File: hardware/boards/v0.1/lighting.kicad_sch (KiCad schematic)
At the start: 18 parts, among them U10 TRIG9, U11 TRIG13, U12 TRIG10, U13 TRIG14, U14 TRIG11, U15 TRIG15, U16 TRIG12, U17 TRIG16, U2 TRIG1, U3 TRIG2, U33 SN74AHCT1G125DBVR, U4 TRIG3, U5 TRIG4, U6 TRIG8, U7 TRIG7, U8 TRIG6, U9 TRIG5

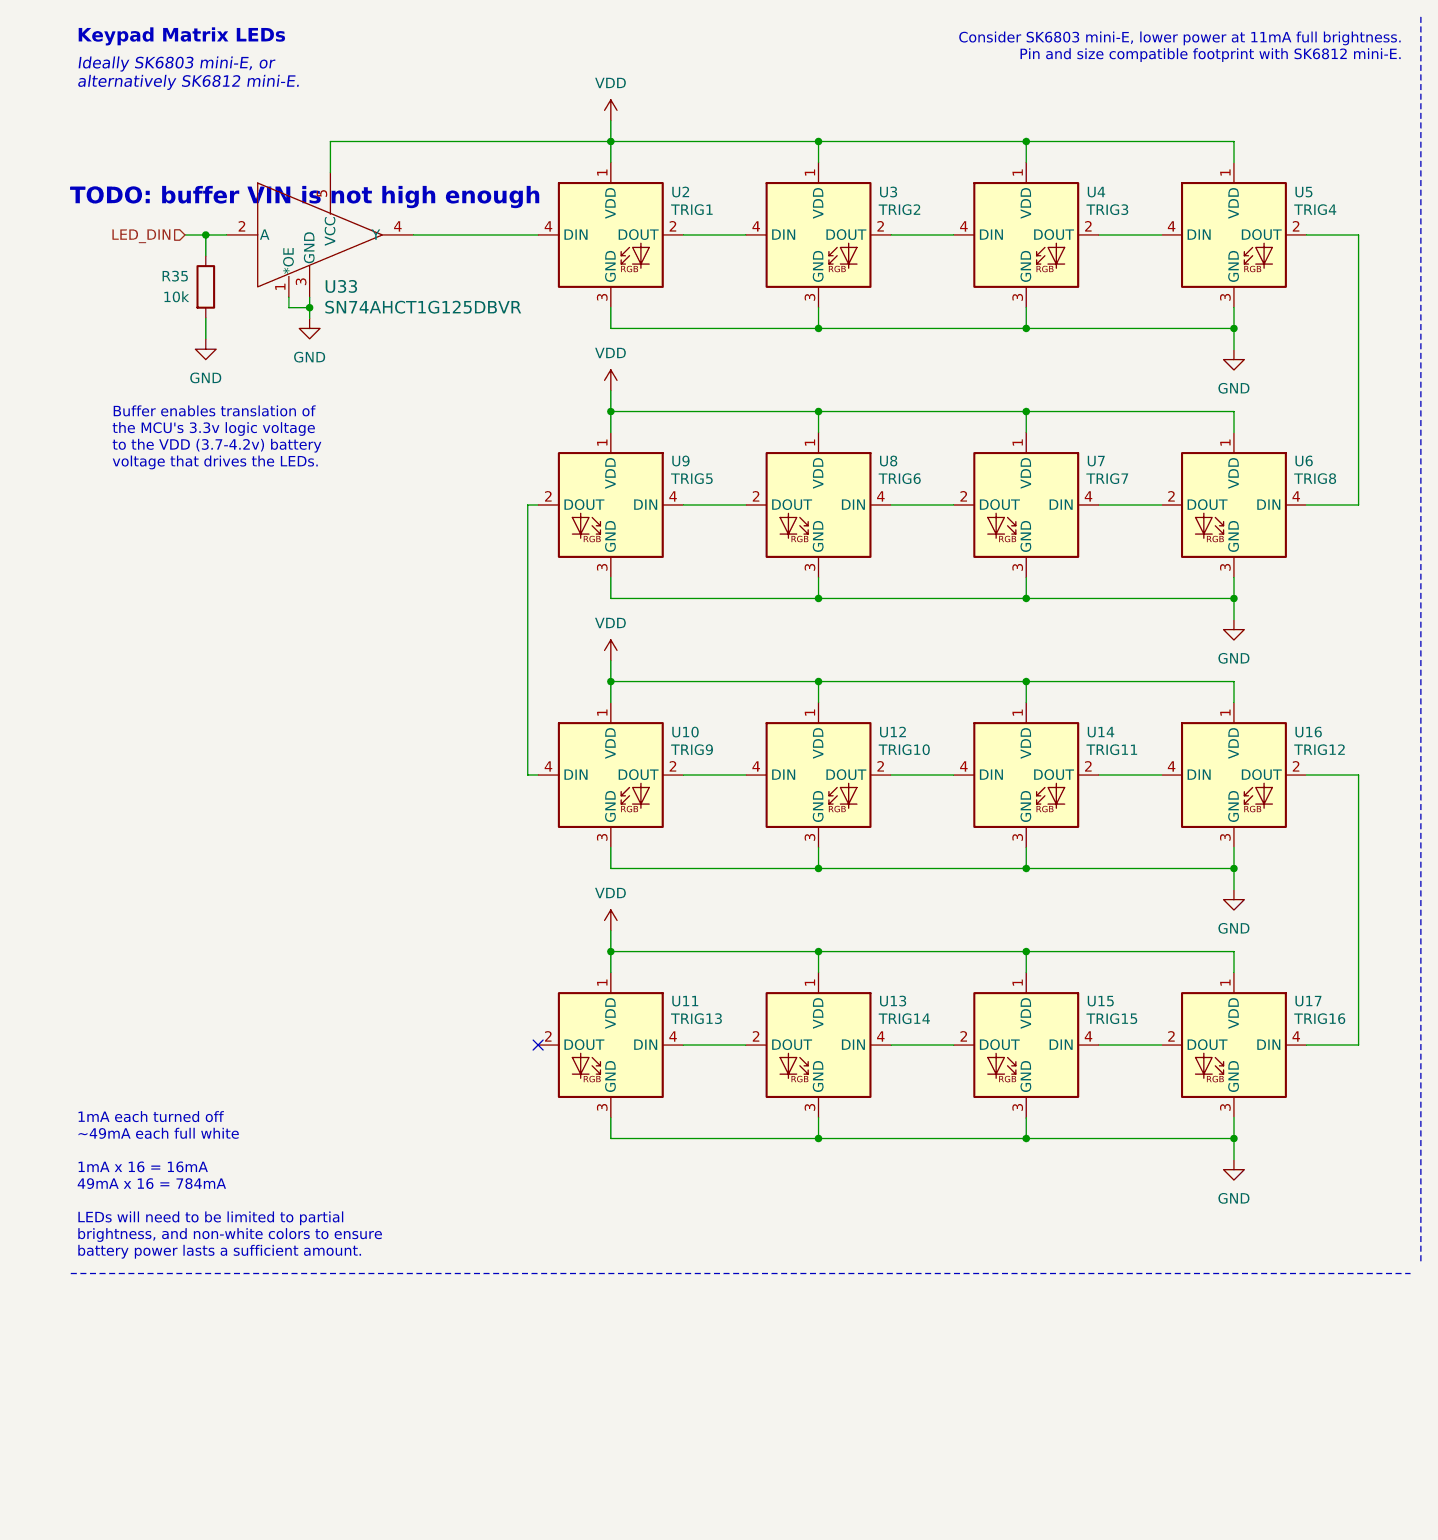
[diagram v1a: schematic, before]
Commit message: feat: fix RGB LED circuit
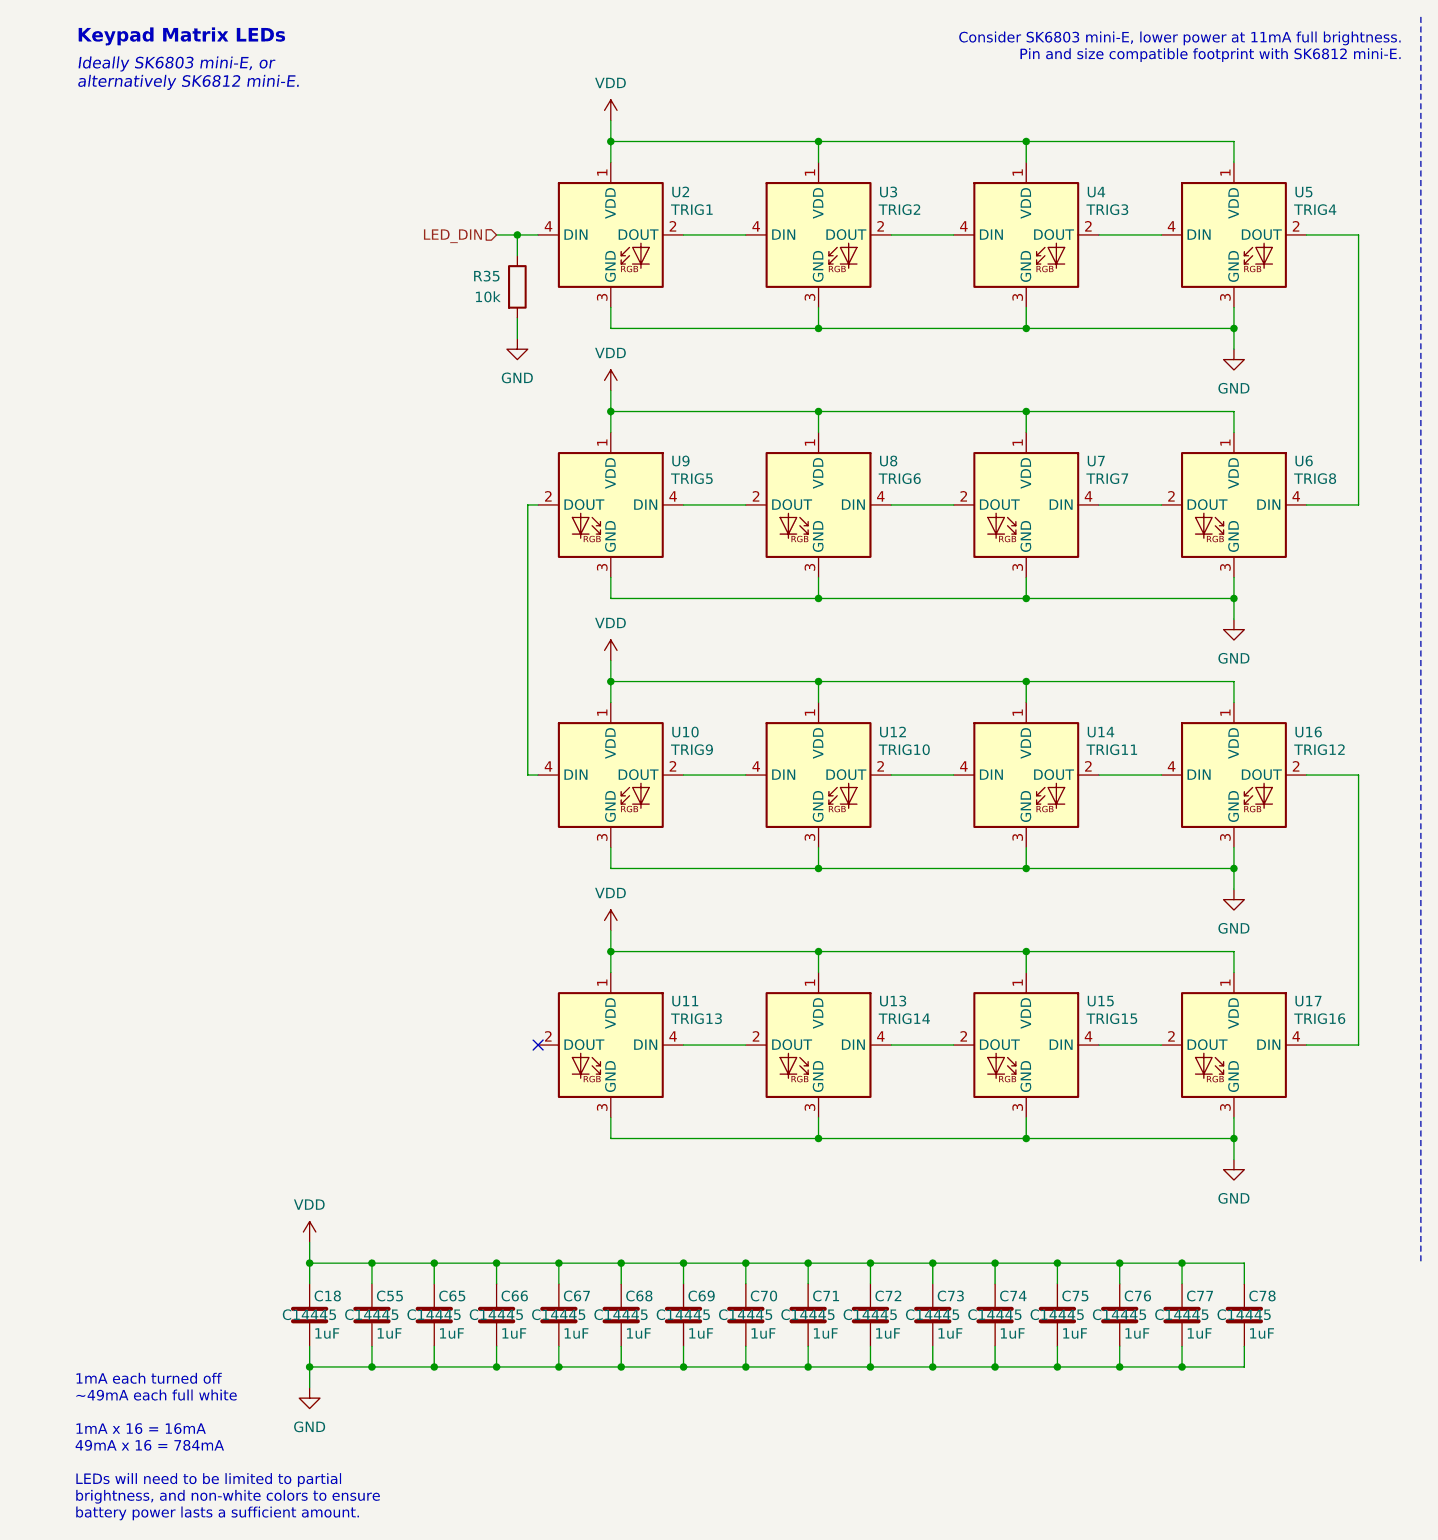
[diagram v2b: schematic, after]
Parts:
- removed U33: SN74AHCT1G125DBVR, pocket_synth:SN74AHCT1G125DBVR, symbol pocket_synth:SN74AHCT1G125DBVR
- added C18, C55, C65, C66, C67, C68, C69, C70, C71, C72, C73, C74, C75, C76, C77, C78: 1uF, Capacitor_SMD:C_0402_1005Metric, symbol Device:C
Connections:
- net GND: now also C18.2, C55.2, C65.2, C66.2, C67.2, C68.2, C69.2, C70.2, C71.2, C72.2, C73.2, C74.2, C75.2, C76.2, C77.2, C78.2
- net LED_DIN: now also U2.4 (DIN)
- net VDD: now also C18.1, C55.1, C65.1, C66.1, C67.1, C68.1, C69.1, C70.1, C71.1, C72.1, C73.1, C74.1, C75.1, C76.1, C77.1, C78.1
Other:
- note removed: "Buffer enables translation of the MCU's 3.3v logic voltage to the VDD (3.7-4.2v) battery voltage that drives the LEDs."
- note removed: "TODO: buffer VIN is not high enough"
- moved on the sheet: R35

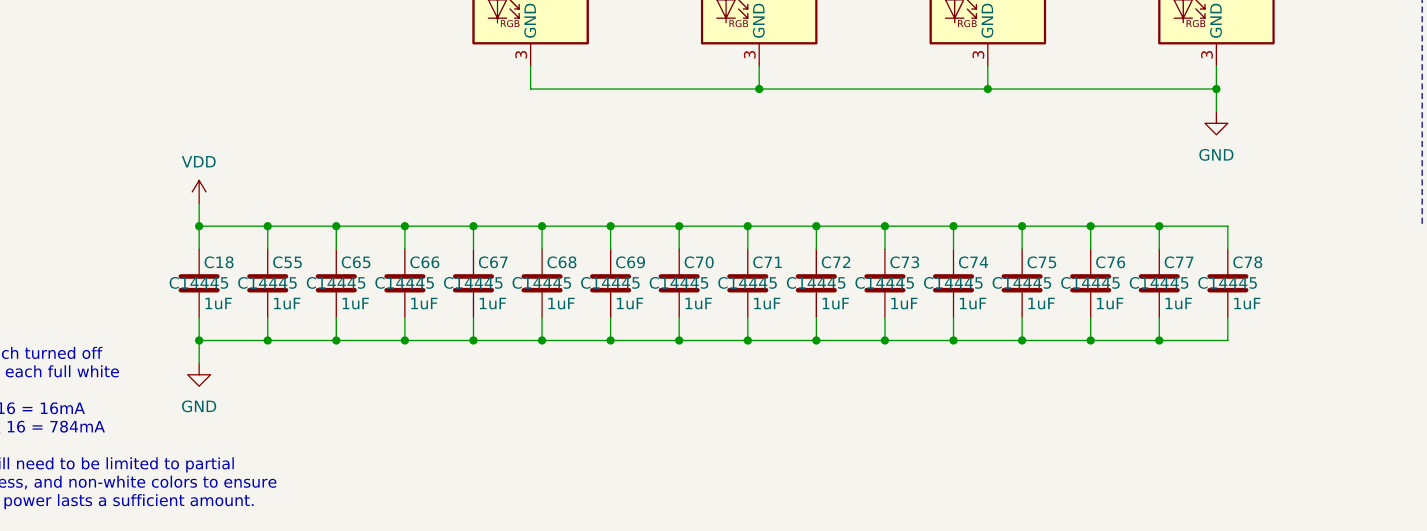
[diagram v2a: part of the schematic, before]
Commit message: feat: change charger, fuel gauge, and battery connector, re-route power system
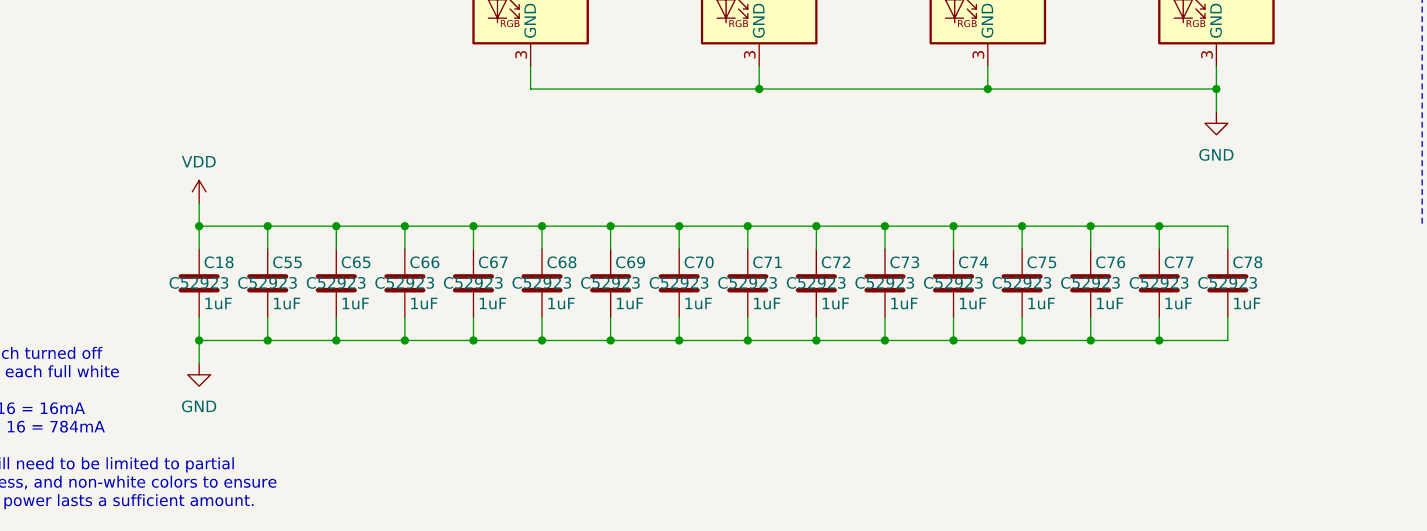
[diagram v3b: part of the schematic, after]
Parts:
- C18, C55, C65, C66, C67, C68, C69, C70, C71, C72, C73, C74, C75, C76, C77, C78: JLC C14445 -> C52923
- R35: JLC C25531 -> C25744
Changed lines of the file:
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@@
 			)
 		)
-		(property "JLC" "C14445"
+		(property "JLC" "C52923"
 			(at 125.73 171.45 0)
 			(effects
@@
 			)
 		)
-		(property "JLC" "C14445"
+		(property "JLC" "C52923"
 			(at 41.91 171.45 0)
 			(effects
@@
 			)
 		)
-		(property "JLC" "C14445"
+		(property "JLC" "C52923"
 			(at 140.97 171.45 0)
 			(effects
@@
 			)
 		)
-		(property "JLC" "C14445"
+		(property "JLC" "C52923"
 			(at 95.25 171.45 0)
 			(effects
@@
 			)
 		)
-		(property "JLC" "C14445"
+		(property "JLC" "C52923"
 			(at 80.01 171.45 0)
 			(effects
@@
 			)
 		)
-		(property "JLC" "C14445"
+		(property "JLC" "C52923"
 			(at 49.53 171.45 0)
 			(effects
@@
 			)
 		)
-		(property "JLC" "C14445"
+		(property "JLC" "C52923"
 			(at 118.11 171.45 0)
 			(effects
@@
 			)
 		)
-		(property "JLC" "C14445"
+		(property "JLC" "C52923"
 			(at 87.63 171.45 0)
 			(effects
@@
 			)
 		)
-		(property "JLC" "C14445"
+		(property "JLC" "C52923"
 			(at 110.49 171.45 0)
 			(effects
@@
 			)
 		)
-		(property "JLC" "C14445"
+		(property "JLC" "C52923"
 			(at 64.77 171.45 0)
 			(effects
@@
 			)
 		)
-		(property "JLC" "C14445"
+		(property "JLC" "C52923"
 			(at 57.15 171.45 0)
 			(effects
@@
 			)
 		)
-		(property "JLC" "C14445"
+		(property "JLC" "C52923"
 			(at 148.59 171.45 0)
 			(effects
@@
 			)
 		)
-		(property "JLC" "C14445"
+		(property "JLC" "C52923"
 			(at 156.21 171.45 0)
 			(effects
@@
 			)
 		)
-		(property "JLC" "C14445"
+		(property "JLC" "C52923"
 			(at 102.87 171.45 0)
 			(effects
@@
 			)
 		)
-		(property "JLC" "C14445"
+		(property "JLC" "C52923"
 			(at 133.35 171.45 0)
 			(effects
@@
 			)
 		)
-		(property "JLC" "C14445"
+		(property "JLC" "C52923"
 			(at 72.39 171.45 0)
 			(effects
@@
 			)
 		)
-		(property "JLC" "C25531"
+		(property "JLC" "C25744"
 			(at 67.31 45.72 0)
 			(effects

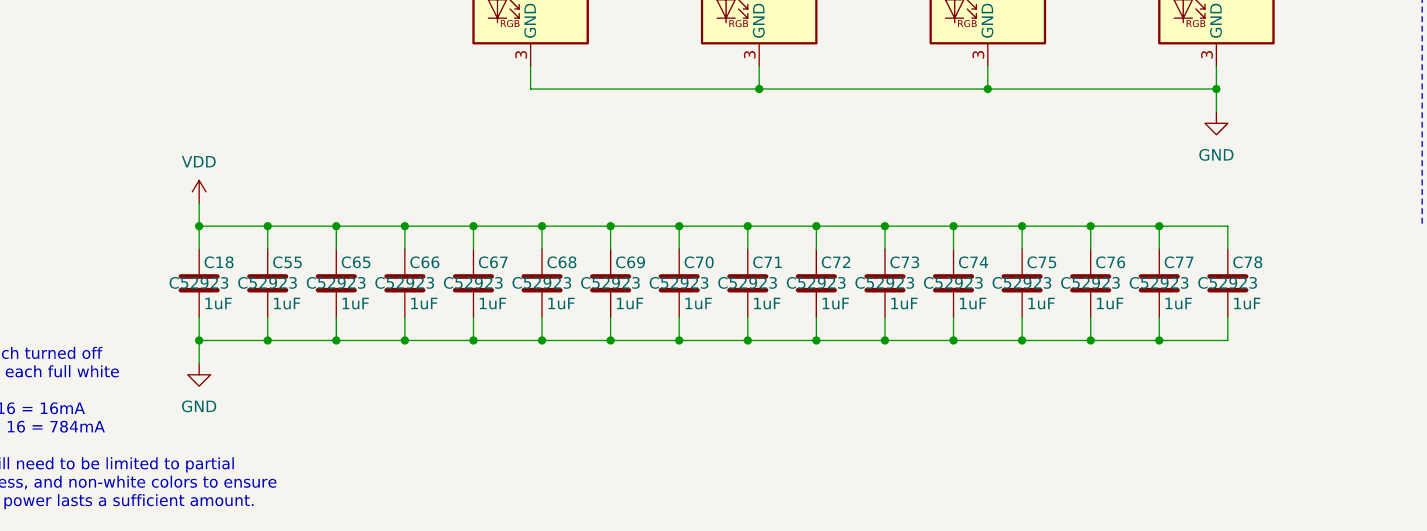
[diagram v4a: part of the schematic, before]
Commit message: feat: various layout and routing adjustments
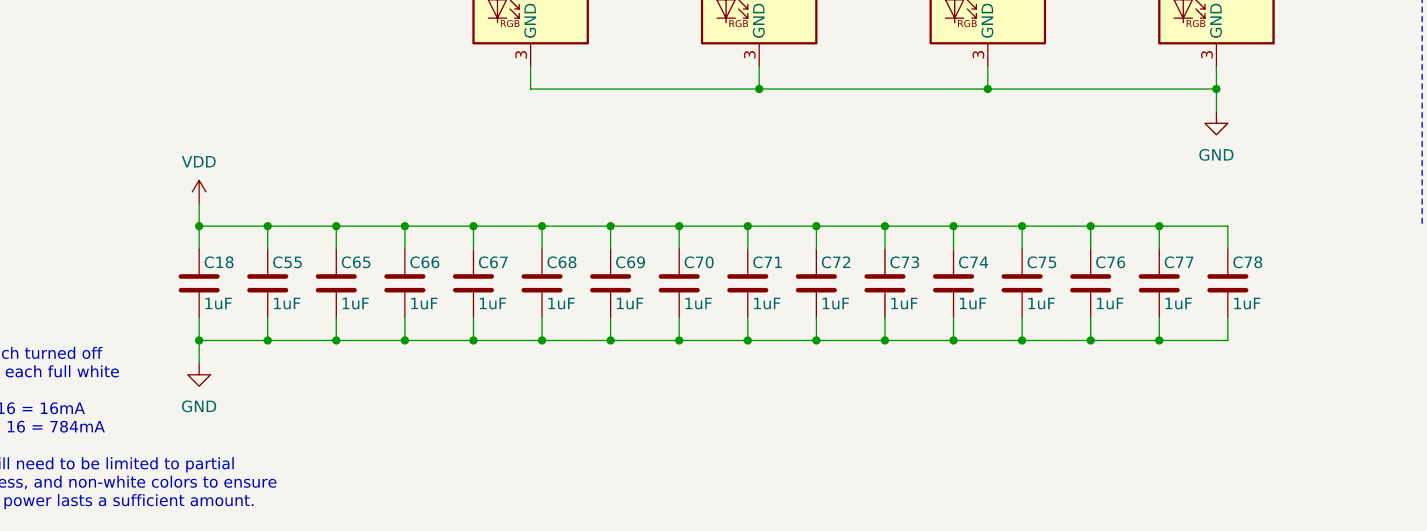
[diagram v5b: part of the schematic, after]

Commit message: fix: rotation offsets and LEDs on wrong side of board
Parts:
- U10, U11, U12, U13, U14, U15, U16, U17, U2, U3, U4, U5, U6, U7, U8, U9: FT Layer Override (none) -> bottom
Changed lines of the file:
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@@
 			)
 		)
+		(property "FT Layer Override" "bottom"
+			(at 104.14 72.39 0)
+			(effects
+				(font
+					(size 1.27 1.27)
+				)
+				(hide yes)
+			)
+		)
 		(pin "2"
 		)
@@
 			)
 		)
+		(property "FT Layer Override" "bottom"
+			(at 78.74 105.41 0)
+			(effects
+				(font
+					(size 1.27 1.27)
+				)
+				(hide yes)
+			)
+		)
 		(pin "2"
 		)
@@
 			)
 		)
+		(property "FT Layer Override" "bottom"
+			(at 154.94 39.37 0)
+			(effects
+				(font
+					(size 1.27 1.27)
+				)
+				(hide yes)
+			)
+		)
 		(pin "2"
 		)
@@
 			)
 		)
+		(property "FT Layer Override" "bottom"
+			(at 129.54 39.37 0)
+			(effects
+				(font
+					(size 1.27 1.27)
+				)
+				(hide yes)
+			)
+		)
 		(pin "2"
 		)
@@
 			)
 		)
+		(property "FT Layer Override" "bottom"
+			(at 129.54 138.43 0)
+			(effects
+				(font
+					(size 1.27 1.27)
+				)
+				(hide yes)
+			)
+		)
 		(pin "2"
 		)
@@
 			)
 		)
+		(property "FT Layer Override" "bottom"
+			(at 154.94 72.39 0)
+			(effects
+				(font
+					(size 1.27 1.27)
+				)
+				(hide yes)
+			)
+		)
 		(pin "2"
 		)
@@
 			)
 		)
+		(property "FT Layer Override" "bottom"
+			(at 78.74 138.43 0)
+			(effects
+				(font
+					(size 1.27 1.27)
+				)
+				(hide yes)
+			)
+		)
 		(pin "2"
 		)
@@
 			)
 		)
+		(property "FT Layer Override" "bottom"
+			(at 78.74 72.39 0)
+			(effects
+				(font
+					(size 1.27 1.27)
+				)
+				(hide yes)
+			)
+		)
 		(pin "2"
 		)
@@
 			)
 		)
+		(property "FT Layer Override" "bottom"
+			(at 104.14 138.43 0)
+			(effects
+				(font
+					(size 1.27 1.27)
+				)
+				(hide yes)
+			)
+		)
 		(pin "2"
 		)
@@
 			)
 		)
+		(property "FT Layer Override" "bottom"
+			(at 129.54 72.39 0)
+			(effects
+				(font
+					(size 1.27 1.27)
+				)
+				(hide yes)
+			)
+		)
 		(pin "2"
 		)
@@
 			)
 		)
+		(property "FT Layer Override" "bottom"
+			(at 154.94 105.41 0)
+			(effects
+				(font
+					(size 1.27 1.27)
+				)
+				(hide yes)
+			)
+		)
 		(pin "2"
 		)
@@
 			)
 		)
+		(property "FT Layer Override" "bottom"
+			(at 104.14 39.37 0)
+			(effects
+				(font
+					(size 1.27 1.27)
+				)
+				(hide yes)
+			)
+		)
 		(pin "2"
 		)
@@
 			)
 		)
+		(property "FT Layer Override" "bottom"
+			(at 104.14 105.41 0)
+			(effects
+				(font
+					(size 1.27 1.27)
+				)
+				(hide yes)
+			)
+		)
 		(pin "2"
 		)
@@
 			)
 		)
+		(property "FT Layer Override" "bottom"
+			(at 78.74 39.37 0)
+			(effects
+				(font
+					(size 1.27 1.27)
+				)
+				(hide yes)
+			)
+		)
 		(pin "2"
 		)
@@
 			)
 		)
+		(property "FT Layer Override" "bottom"
+			(at 154.94 138.43 0)
+			(effects
+				(font
+					(size 1.27 1.27)
+				)
+				(hide yes)
+			)
+		)
 		(pin "2"
 		)
@@
 			(at 129.54 105.41 0)
 			(effects
+				(font
+					(size 1.27 1.27)
+				)
+				(hide yes)
+			)
+		)
+		(property "FT Layer Override" "bottom"
+			(at 129.54 105.41 0)
+			(effects
